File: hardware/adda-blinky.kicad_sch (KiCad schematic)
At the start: 18 parts, among them J1 Conn_01x02, J2 Conn_01x02, J3 USB_B_Micro, J4 Conn_01x02, U1 ATtiny1616-S, U2 ATtiny1616-M, U3 AMS1117-3.3

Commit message: First order
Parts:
- removed C2: 1u, Capacitor_SMD:C_0805_2012Metric, symbol Device:C
- removed D8: D_Schottky, symbol Device:D_Schottky
- removed J3: USB_B_Micro, Connector_USB:USB_Micro-AB_Molex_47590-0001, symbol Connector:USB_B_Micro
- removed J4: Conn_01x02, Connector_Molex:Molex_KK-254_AE-6410-02A_1x02_P2.54mm_Vertical, symbol Connector_Generic:Conn_01x02
- removed U1: ATtiny1616-S, Package_SO:SOIC-20W_7.5x12.8mm_P1.27mm, symbol MCU_Microchip_ATtiny:ATtiny1616-S
- removed U3: AMS1117-3.3, Package_TO_SOT_SMD:SOT-223-3_TabPin2, symbol Regulator_Linear:AMS1117-3.3
- added C5: 1u, Capacitor_SMD:C_0805_2012Metric, symbol Device:C
- added D10: 1N5819, Diode_SMD:D_SOD-323, symbol Device:D_Schottky
- added H1: MountingHole, MountingHole:MountingHole_3.2mm_M3_Pad, symbol Mechanical:MountingHole
- added H2, H3, H4: MountingHole, symbol Mechanical:MountingHole
- added J3: PB5, Connector_Molex:Molex_KK-254_AE-6410-02A_1x02_P2.54mm_Vertical, symbol Connector_Generic:Conn_01x02
- added J4: COMM, Connector_Molex:Molex_KK-254_AE-6410-05A_1x05_P2.54mm_Vertical, symbol Connector_Generic:Conn_01x05
- added J5: PWR, Connector_Molex:Molex_KK-254_AE-6410-03A_1x03_P2.54mm_Vertical, symbol Connector_Generic:Conn_01x03
- added R0, R1, R2, R3, R4, R5, R6, R7, R8: 220, Resistor_SMD:R_0805_2012Metric, symbol Device:R
- added RV1: R_Potentiometer, Connector_PinHeader_2.54mm:PinHeader_1x03_P2.54mm_Vertical, symbol Device:R_Potentiometer
- J1: value Conn_01x02 -> AIN
- J2: value Conn_01x02 -> AOUT
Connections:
- net GND: now also J1.1 (Pin_1), C5.2, J3.1 (Pin_1), J4.1 (Pin_1), J5.2 (Pin_2), RV1.3; no longer J1.2 (Pin_2)
- net PA1/MOSI/SDA: now also J4.5 (Pin_5)
- net PA2/MISO/SCL: now also J4.4 (Pin_4)
- net PA3/SCK: now also J4.3 (Pin_3)
- net PA4/SS: now also J4.2 (Pin_2)
- net PA5/AIN5: now also J1.2 (Pin_2); no longer J1.1 (Pin_1)
- net PB0: now also R4.1; no longer D4.1 (K)
- net PB1: now also R5.1; no longer D5.1 (K)
- net PB2: now also R6.1; no longer D6.1 (K)
- net PB3: now also R7.1; no longer D7.1 (K)
- net PB4: now also C1.1, RV1.2
- net PB5: now also J3.2 (Pin_2)
- net PC0: now also R0.1; no longer D0.1 (K)
- net PC1: now also R1.1; no longer D1.1 (K)
- net PC2: now also R2.1; no longer D2.1 (K)
- net PC3: now also R3.1; no longer D3.1 (K)
- net ~{RESET}: now also R8.1
- net +3.3V renamed +5V
- net +5V: now also C5.1, D10.1 (K), RV1.1; no longer C1.1
- new net: D6.1 (K), R6.2
- new net: D7.1 (K), R7.2
- new net: D2.1 (K), R2.2
- new net: D10.2 (A), J5.1 (Pin_1)
- new net: D5.1 (K), R5.2
- new net: D3.1 (K), R3.2
- new net: D0.1 (K), R0.2
- new net: D4.1 (K), R4.2
- new net: D1.1 (K), R1.2
- new net UPDI: J5.3 (Pin_3), R8.2
- no-connect marks 3 -> 1
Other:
- moved on the sheet: D0, D1, D2, D3, D4, D5, D6, D7, J1, J2, U2

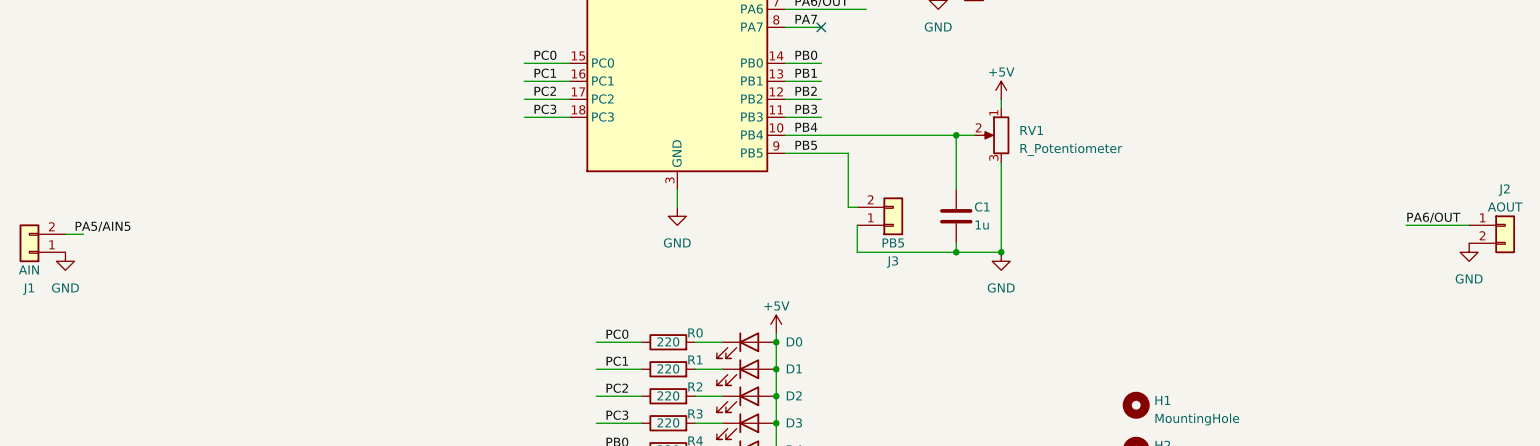
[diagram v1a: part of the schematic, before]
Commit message: Add series resistors to I/Os
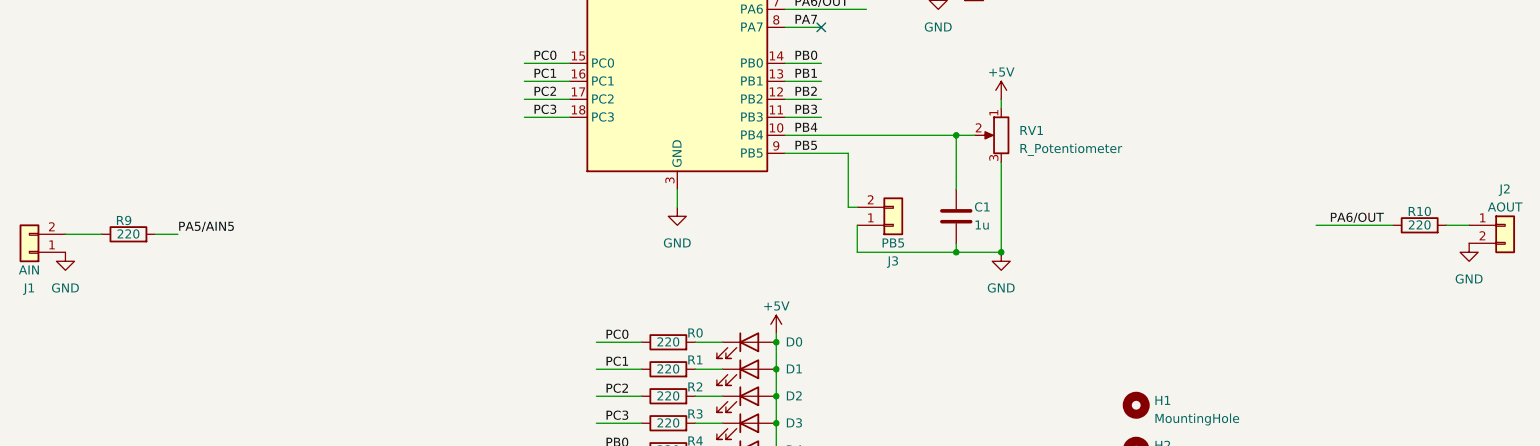
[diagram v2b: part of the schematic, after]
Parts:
- added R10, R9: 220, Resistor_SMD:R_0805_2012Metric, symbol Device:R
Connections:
- net PA5/AIN5: now also R9.2; no longer J1.2 (Pin_2)
- net PA6/OUT: now also R10.1; no longer J2.1 (Pin_1)
- new net: J2.1 (Pin_1), R10.2
- new net: J1.2 (Pin_2), R9.1
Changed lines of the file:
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@@
-    (stroke (width 0) (type default))
-  )
-  (wire (pts (xy 41.91 90.17) (xy 39.37 90.17))
     (stroke (width 0) (type default))
   )
@@
     (stroke (width 0) (type default))
   )
+  (wire (pts (xy 39.37 90.17) (xy 44.45 90.17))
+    (stroke (width 0) (type default))
+  )
   (wire (pts (xy 140.97 43.18) (xy 156.21 43.18))
     (stroke (width 0) (type default))
@@
     (stroke (width 0) (type default))
   )
-  (wire (pts (xy 228.6 88.9) (xy 237.49 88.9))
-    (stroke (width 0) (type default))
-  )
   (wire (pts (xy 171.45 80.01) (xy 171.45 92.71))
     (stroke (width 0) (type default))
@@
     (stroke (width 0) (type default))
   )
+  (wire (pts (xy 234.315 88.9) (xy 237.49 88.9))
+    (stroke (width 0) (type default))
+  )
   (wire (pts (xy 55.88 35.56) (xy 55.88 38.1))
     (stroke (width 0) (type default))
@@
     (stroke (width 0) (type default))
   )
+  (wire (pts (xy 215.9 88.9) (xy 226.695 88.9))
+    (stroke (width 0) (type default))
+  )
   (wire (pts (xy 140.97 71.12) (xy 146.05 71.12))
     (stroke (width 0) (type default))
@@
     (stroke (width 0) (type default))
   )
+  (wire (pts (xy 52.07 90.17) (xy 55.245 90.17))
+    (stroke (width 0) (type default))
+  )
   (wire (pts (xy 140.97 50.8) (xy 162.56 50.8))
     (stroke (width 0) (type default))
@@
     (effects (font (size 1.27 1.27)) (justify left bottom))
   )
-  (label "PA6{slash}OUT" (at 228.6 88.9 0) (fields_autoplaced)
+  (label "PA6{slash}OUT" (at 217.805 88.9 0) (fields_autoplaced)
     (effects (font (size 1.27 1.27)) (justify left bottom))
   )
@@
     (effects (font (size 1.27 1.27)) (justify left bottom))
   )
-  (label "PA5{slash}AIN5" (at 40.64 90.17 0) (fields_autoplaced)
+  (label "PA5{slash}AIN5" (at 55.245 90.17 0) (fields_autoplaced)
     (effects (font (size 1.27 1.27)) (justify left bottom))
   )
@@
         (path "/aa8d4fa8-9a28-4180-b4ba-75e5c4d6859f"
           (reference "#PWR09") (unit 1)
+        )
+      )
+    )
+  )
+  (symbol (lib_id "Device:R") (at 230.505 88.9 90) (unit 1)
+    (in_bom yes) (on_board yes) (dnp no)
+    (property "Reference" "R10" (at 230.505 86.995 90)
+      (effects (font (size 1.27 1.27)))
+    )
+    (property "Value" "220" (at 230.505 88.9 90)
+      (effects (font (size 1.27 1.27)))
+    )
+    (property "Footprint" "Resistor_SMD:R_0805_2012Metric" (at 230.505 90.678 90)
+      (effects (font (size 1.27 1.27)) hide)
+    )
+    (property "Datasheet" "~" (at 230.505 88.9 0)
+      (effects (font (size 1.27 1.27)) hide)
+    )
+    (pin "1")
+    (pin "2")
+    (instances
+      (project "adda-blinky"
+        (path "/aa8d4fa8-9a28-4180-b4ba-75e5c4d6859f"
+          (reference "R10") (unit 1)
         )
       )
@@
         )
       )
+    )
+  )
+  (symbol (lib_id "Device:R") (at 48.26 90.17 90) (unit 1)
+    (in_bom yes) (on_board yes) (dnp no)
+    (property "Reference" "R9" (at 47.625 88.265 90)
+      (effects (font (size 1.27 1.27)))
+    )
+    (property "Value" "220" (at 48.26 90.17 90)
+      (effects (font (size 1.27 1.27)))
+    )
+    (property "Footprint" "Resistor_SMD:R_0805_2012Metric" (at 48.26 91.948 90)
+      (effects (font (size 1.27 1.27)) hide)
+    )
+    (property "Datasheet" "~" (at 48.26 90.17 0)
+      (effects (font (size 1.27 1.27)) hide)
+    )
+    (pin "1")
+    (pin "2")
+    (instances
+      (project "adda-blinky"
+        (path "/aa8d4fa8-9a28-4180-b4ba-75e5c4d6859f"
+          (reference "R9") (unit 1)
+        )
+      )

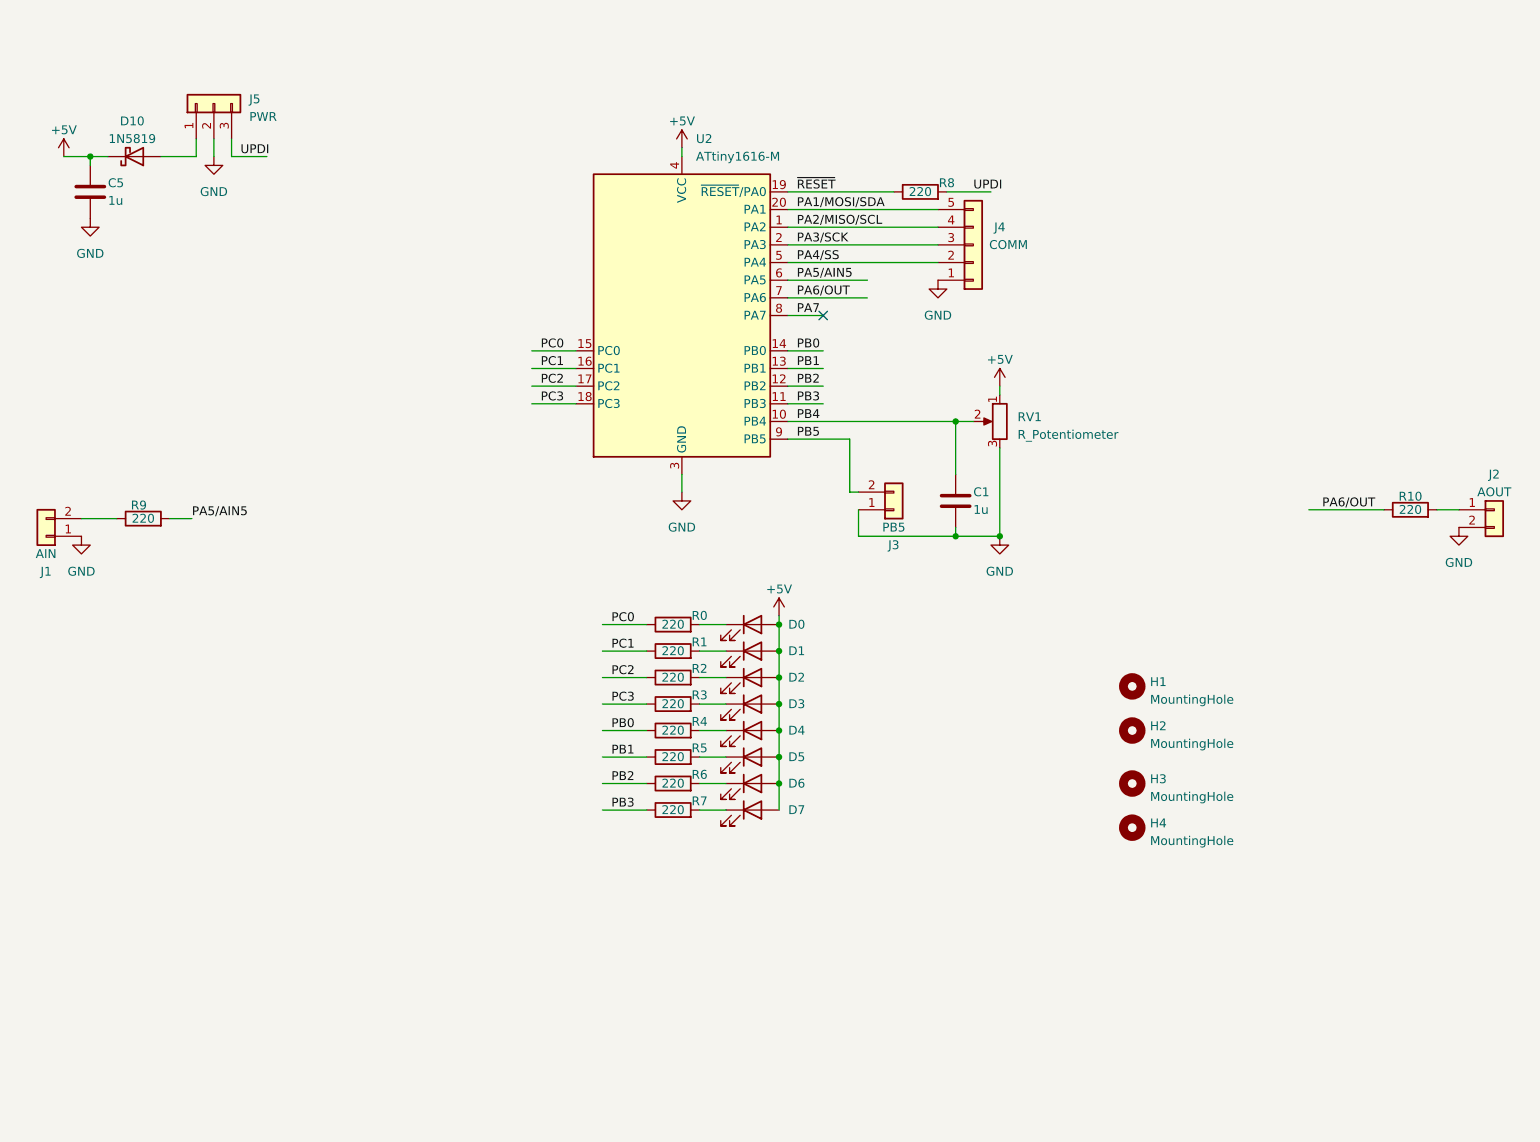
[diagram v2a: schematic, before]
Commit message: Add LED to PB5 for status and sample indicator
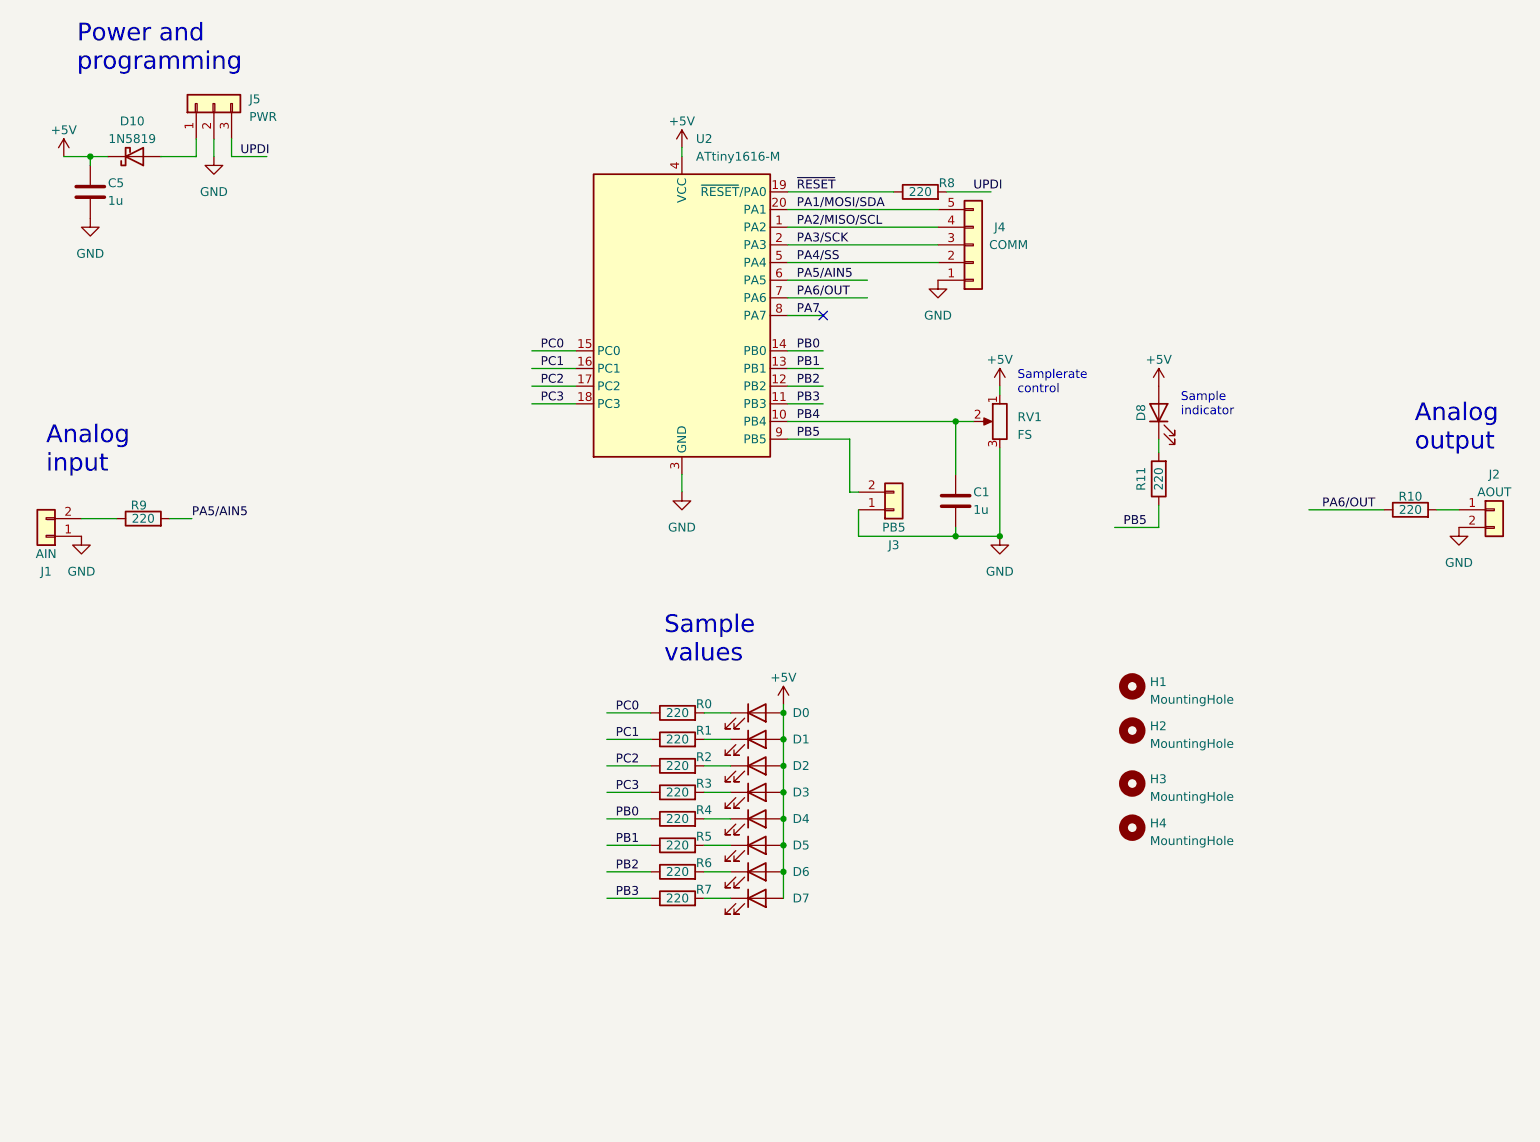
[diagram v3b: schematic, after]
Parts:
- added D8: LED, Diode_SMD:D_0805_2012Metric, symbol Device:LED
- added R11: 220, Resistor_SMD:R_0805_2012Metric, symbol Device:R
- RV1: value R_Potentiometer -> FS
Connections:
- net +5V: now also D8.2 (A)
- net PB5: now also R11.1
- new net: D8.1 (K), R11.2
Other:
- note added: "Analog input"
- note added: "Analog output"
- note added: "Power and programming"
- note added: "Sample indicator"
- note added: "Sample values"
- note added: "Samplerate control"
- moved on the sheet: D0, D1, D2, D3, D4, D5, D6, D7, R0, R1, R2, R3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
